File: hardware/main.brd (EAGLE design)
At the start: 95.2 x 80.4 mm, 107 parts, among them IC1 MPU-6050, IC2 TB6612FNG, M1 MOTOR_MOUNT_V2, M2 LED_MOUNT, M3 LED_MOUNT, M4 LED_MOUNT, M5 LED_MOUNT, M6 LED_MOUNT, M7 LED_MOUNT, Q7 IRLML2244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

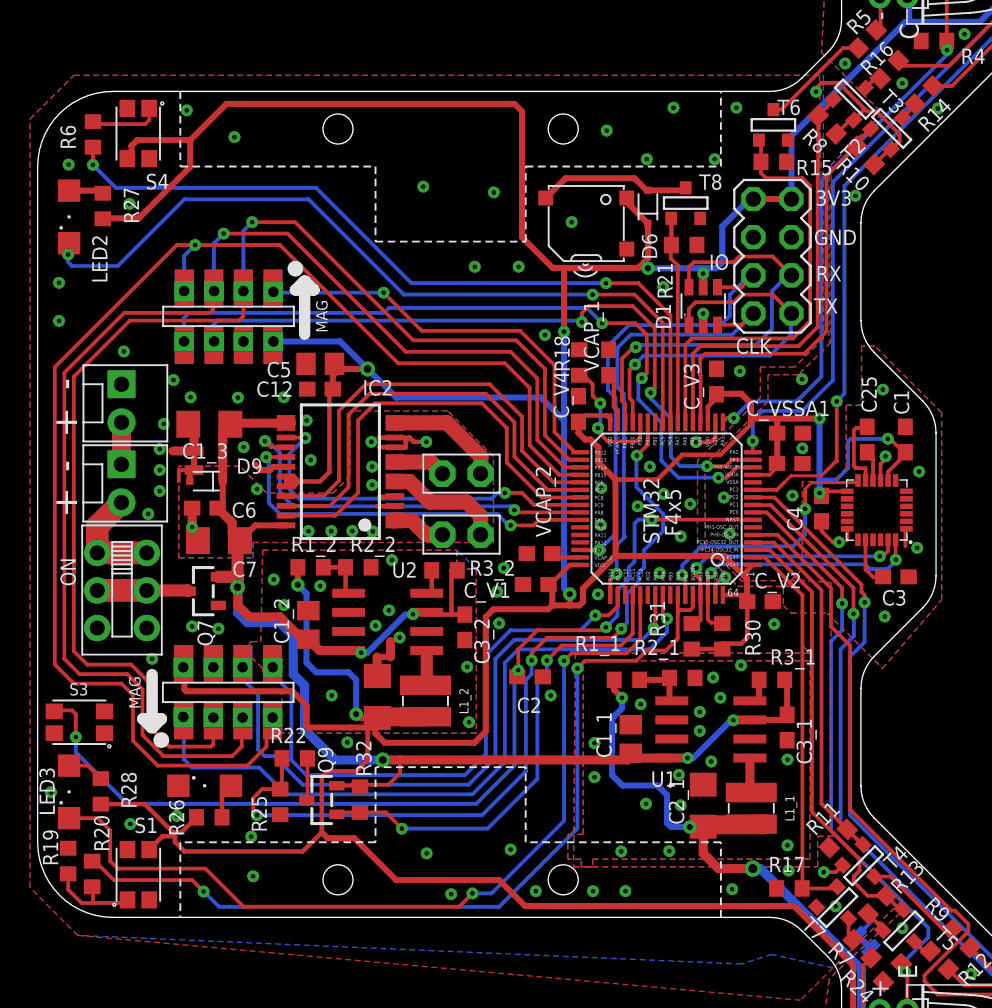
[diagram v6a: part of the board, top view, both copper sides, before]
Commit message: moved step down converters closer to battery
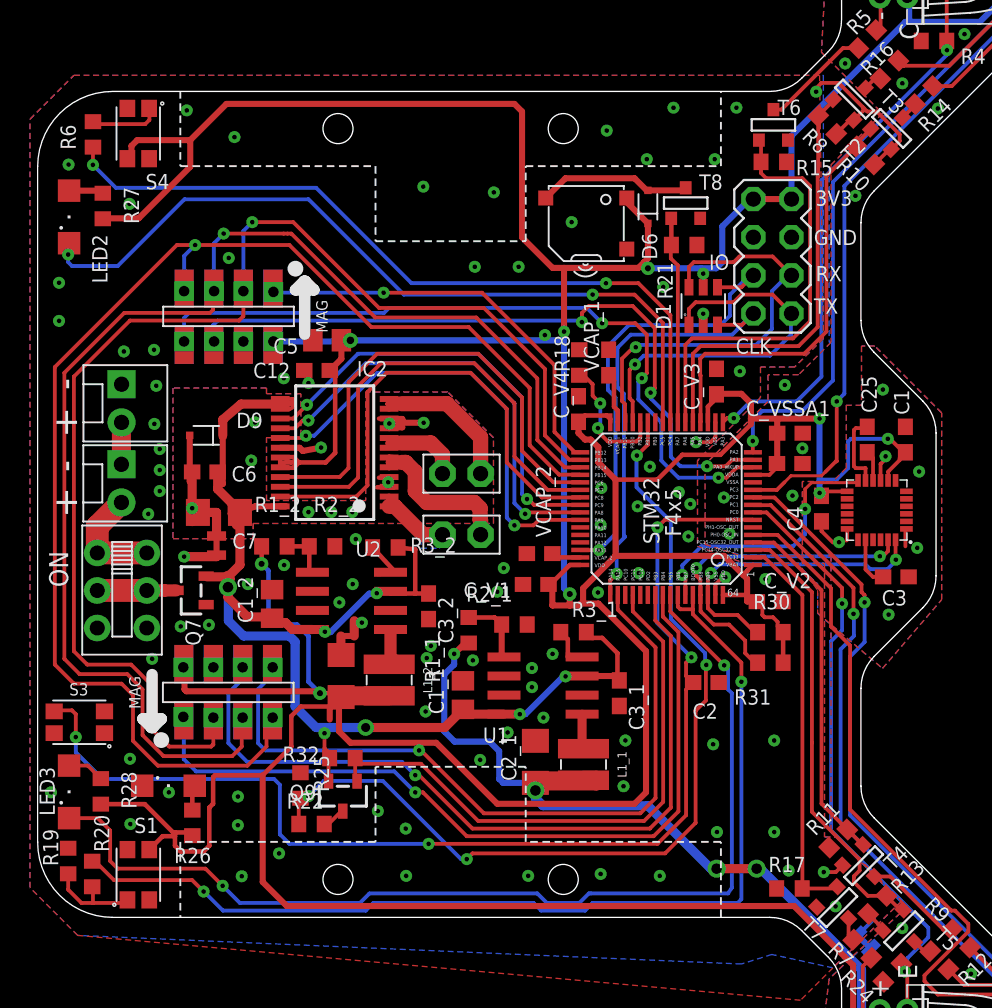
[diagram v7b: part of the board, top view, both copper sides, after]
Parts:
- removed C1_3: 10u, rcl:C1206
- moved R3_1 13.6 mm to (35.7, -8.51)
- moved R2_1 11.7 mm to (31.8, -8.00)
- moved C2 11.7 mm to (44.5, -11.9)
- moved C2_1 11.6 mm to (33.1, -17.1)
- moved L1_1 11.6 mm to (36.3, -17.3)
- moved U1 11.6 mm to (33.7, -12.1)
- moved C1_1 11.6 mm to (28.3, -12.7)
- moved C3_1 11.4 mm to (38.7, -12.6)
- moved R1_1 11.0 mm to (28.7, -8.38), turned to 270 degrees
- moved PT2 5.86 mm to (11.9, -2.74), turned to 180 degrees
- moved R31 5.52 mm to (48.8, -10.5), turned to 0 degrees
- moved R22 4.51 mm to (18.2, -21.3)
- moved R3_2 4.22 mm to (23.2, -2.87)
- moved R30 3.21 mm to (48.8, -8.51), turned to 0 degrees
- moved D9 3.05 mm to (11.2, 4.60)
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- renumbered ON to OFF
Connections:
- net +7V: no longer C1_3.1
- net GND: no longer C1_3.2
- net LED3: now also U3.PB5; no longer U3.PC12
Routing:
- net +3V3: track 522.2 -> 539.6 mm
- net VCC: track 206.3 -> 218.7 mm, vias 3 -> 4
- net LED3: track 58.3 -> 69.9 mm
- net RST: track 66.2 -> 77.2 mm
- net ENCR_A: track 38.4 -> 49.1 mm
- net BOOT0: track 58.8 -> 68.8 mm
- net +7V: track 101.4 -> 92.3 mm, vias 6 -> 7
- net ENCR_B: track 43.9 -> 52.7 mm
- net GNDA: track 12.7 -> 20.7 mm, vias 10 -> 9
- net DIV_EN: track 32.4 -> 39.0 mm, vias 2 -> 0
- net SPI2_CS2: track 46.7 -> 53.2 mm
- net ADC_VBAT: track 55.4 -> 61.4 mm
- net MR_IN1: track 26.0 -> 30.8 mm
- net I2C1_SCL: track 18.3 -> 22.7 mm
- net MR_PWM: track 25.3 -> 29.7 mm
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
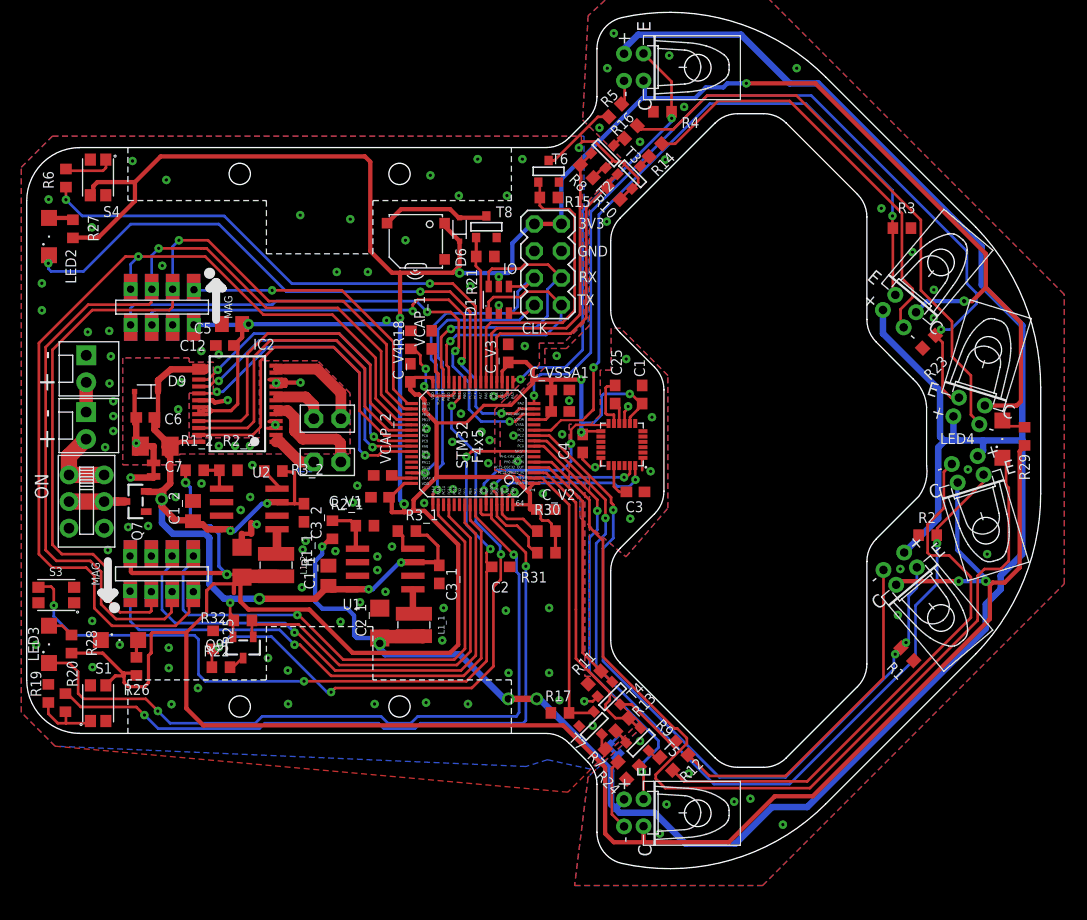
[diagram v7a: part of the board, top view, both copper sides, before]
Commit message: add more GND vias, models
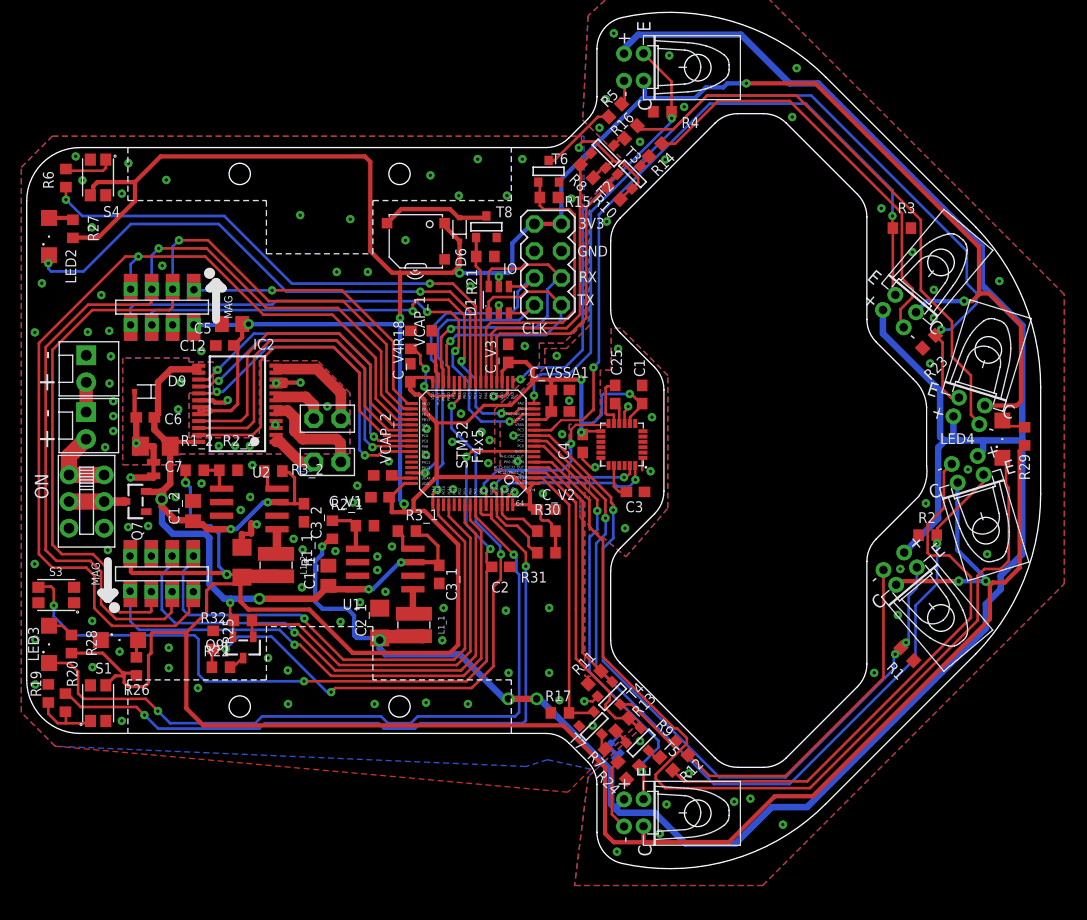
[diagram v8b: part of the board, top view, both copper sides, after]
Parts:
- moved PT2 0.06 mm to (11.9, -2.68)
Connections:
- net VCC renamed +1.8V
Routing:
- net +7V: track 92.3 -> 86.3 mm
- net GNDA: track 20.7 -> 16.2 mm, vias 9 -> 10
- net +3V3: track 539.6 -> 538.7 mm
- net GND: track 42.6 -> 42.7 mm, vias 96 -> 100
